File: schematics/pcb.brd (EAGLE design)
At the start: 69.8 x 100 mm, 39 parts, among them IC1 7805TV, IC2 4050D, IC3 LP298XS, Q1 16Mhz, Q2 16Mhz, X1 MICROSD

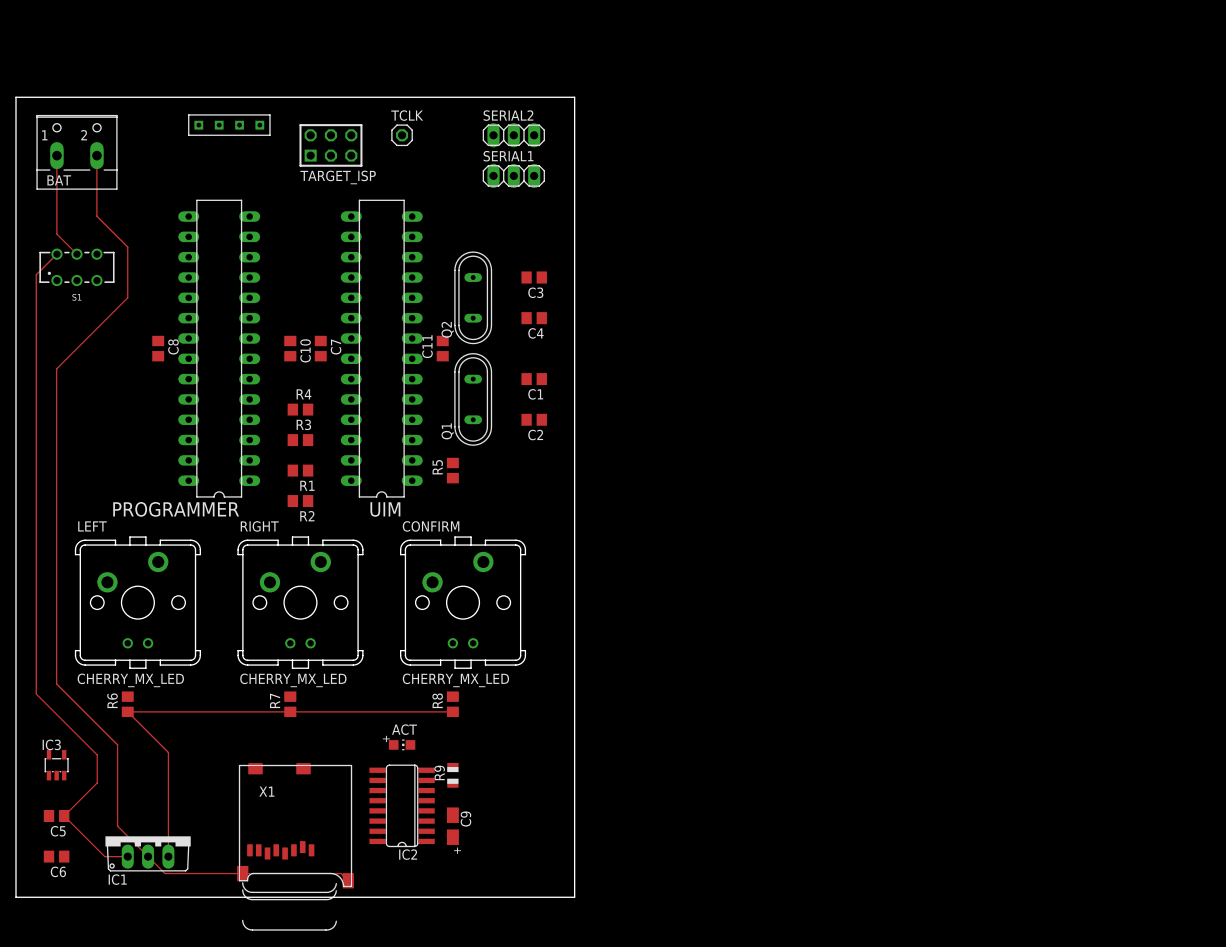
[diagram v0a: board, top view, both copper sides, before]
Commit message: Updated OLED module in part library; Scraped current PCB placements
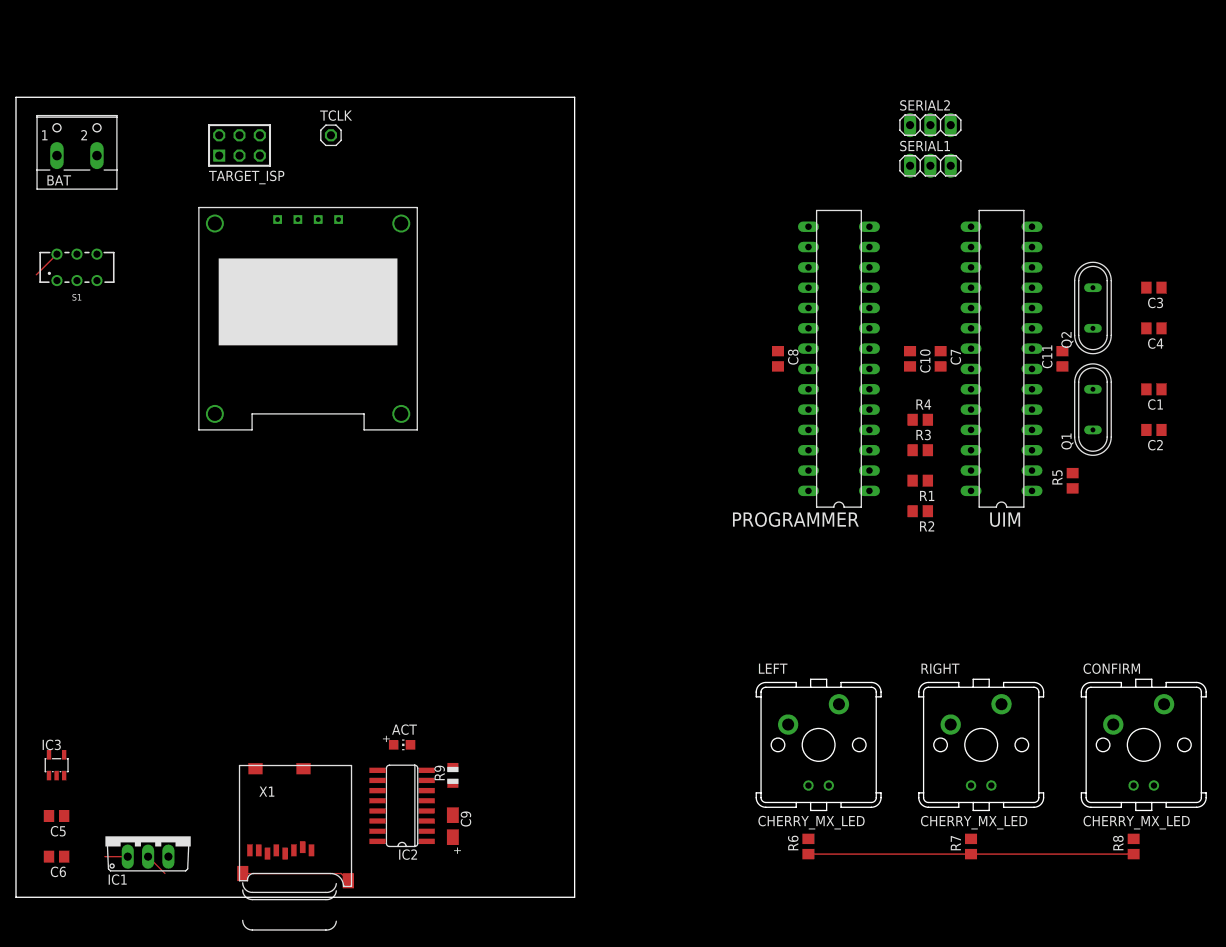
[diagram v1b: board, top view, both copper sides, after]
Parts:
- moved CONFIRM 86.9 mm to (141.0, 19.1)
- moved LEFT 86.9 mm to (100.3, 19.1)
- moved R6 86.9 mm to (99.1, 6.35)
- moved R7 86.9 mm to (119.4, 6.35)
- moved RIGHT 86.9 mm to (120.7, 19.1)
- moved R8 86.9 mm to (139.7, 6.35)
- moved C1 77.5 mm to (142.2, 63.5)
- moved C2 77.5 mm to (142.2, 58.4)
- moved C3 77.5 mm to (142.2, 76.2)
- moved C4 77.5 mm to (142.2, 71.1)
- moved R5 77.5 mm to (132.1, 52.1)
- moved C10 77.5 mm to (111.8, 67.3)
- moved C11 77.5 mm to (130.8, 67.3)
- moved C7 77.5 mm to (115.6, 67.3)
- moved C8 77.5 mm to (95.2, 67.3)
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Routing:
- net GND: track 123.9 -> 16.6 mm
- net PWRIN: track 86.2 -> 6.51 mm
- net +5V: track 60.8 -> 40.6 mm
- net N$17: track 13.4 -> 0.00 mm

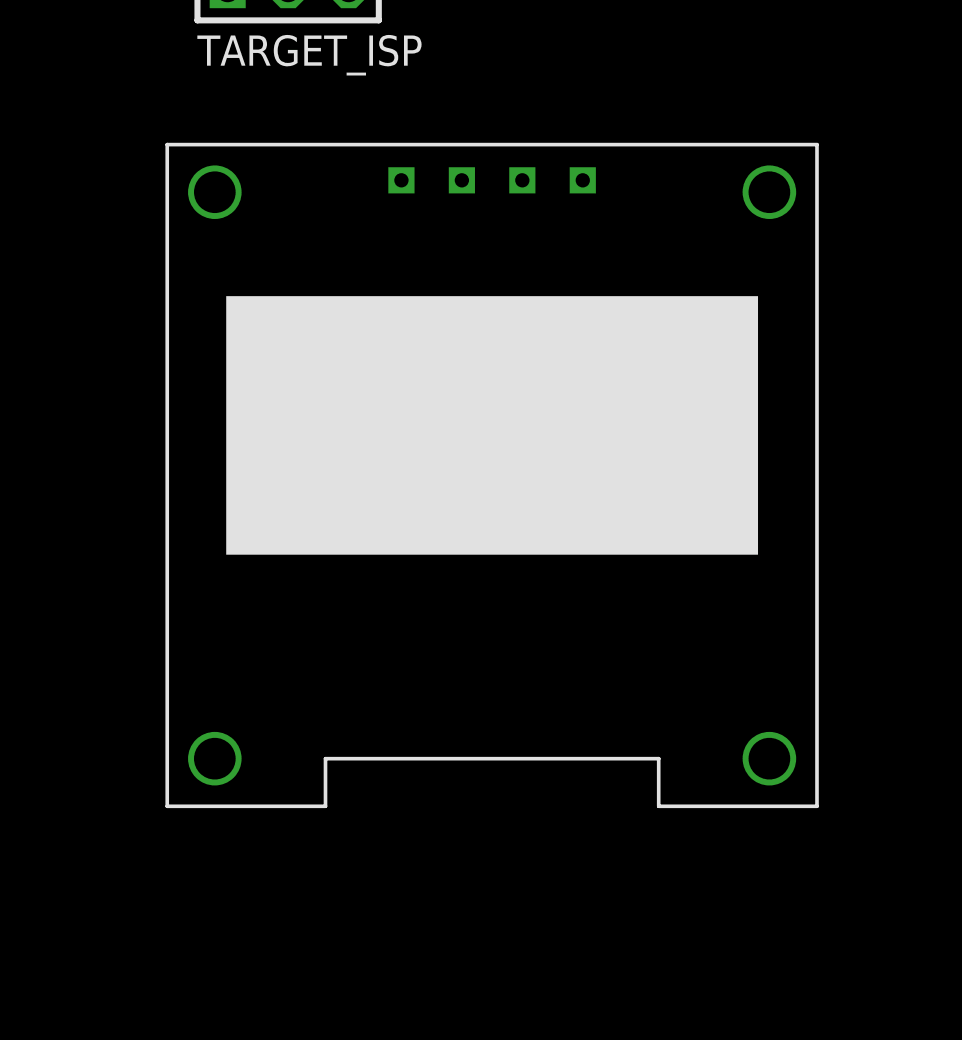
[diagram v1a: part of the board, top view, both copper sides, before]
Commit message: Further updates to OLED module
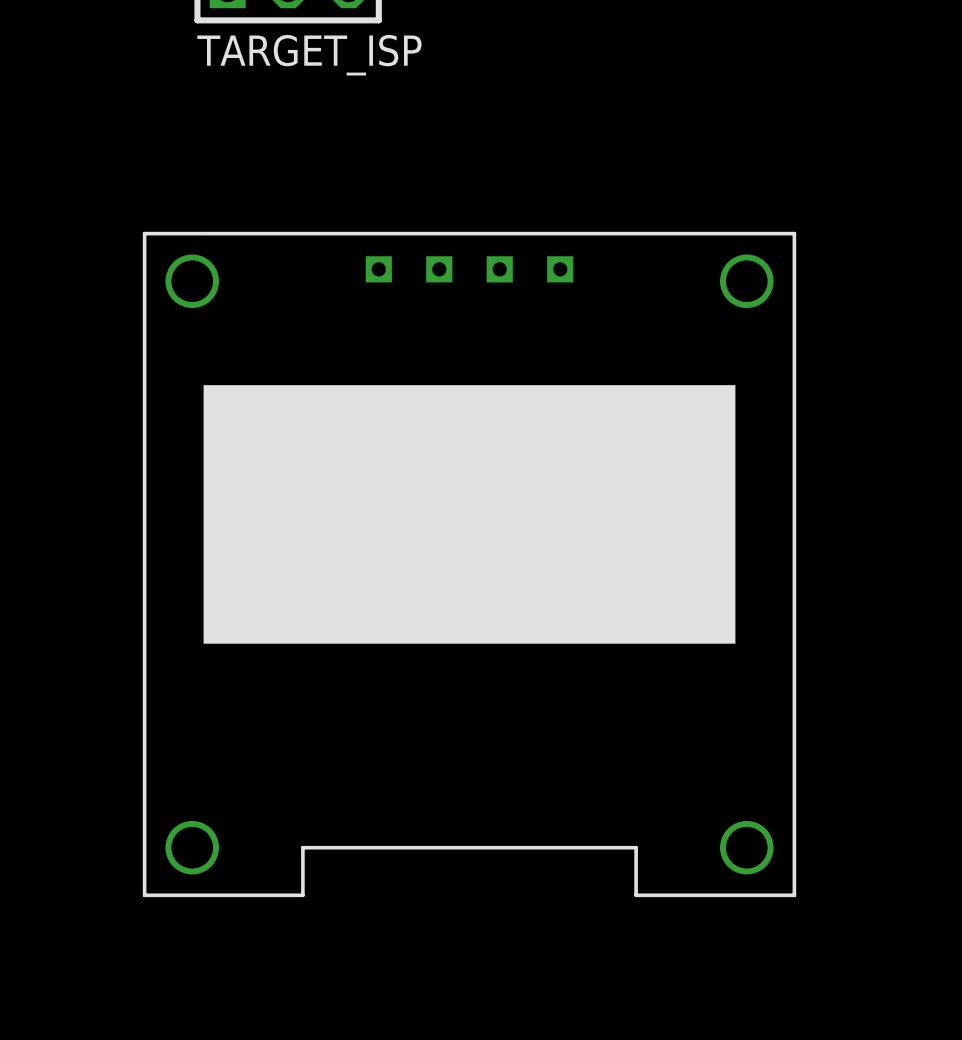
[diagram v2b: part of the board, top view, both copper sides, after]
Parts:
- moved U$1 16.3 mm to (35.6, 68.6)
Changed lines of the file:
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@@
 </autorouter>
 <elements>
-<element name="ACT" library="adafruit" package="CHIP-LED0805" value="RED" x="48.26" y="19.05" smashed="yes" rot="R270">
+<element name="ACT" library="adafruit" library_urn="urn:adsk.eagle:library:420" package="CHIP-LED0805" package3d_urn="urn:adsk.eagle:package:6240557/1" value="RED" x="48.26" y="19.05" smashed="yes" rot="R270">
 <attribute name="NAME" x="46.99" y="20.32" size="1.27" layer="25"/>
 <attribute name="VALUE" x="46.99" y="16.51" size="1.27" layer="27"/>
@@
 <attribute name="VALUE" x="92.71" y="68.58" size="1.27" layer="27" rot="R270"/>
 </element>
-<element name="C9" library="adafruit" package="A/3216-18R" value="10uF" x="54.61" y="8.89" smashed="yes" rot="R270">
+<element name="C9" library="adafruit" library_urn="urn:adsk.eagle:library:420" package="A/3216-18R" package3d_urn="urn:adsk.eagle:package:6240466/1" value="10uF" x="54.61" y="8.89" smashed="yes" rot="R270">
 <attribute name="NAME" x="55.61" y="10.84" size="1.27" layer="25" rot="R270"/>
 <attribute name="VALUE" x="52.285" y="10.84" size="1.27" layer="27" rot="R270"/>
@@
 <attribute name="VALUE" x="11.43" y="0" size="1.27" layer="27" ratio="10"/>
 </element>
-<element name="IC2" library="40xx" package="SO16" value="4050D" x="48.26" y="11.43" smashed="yes" rot="R90">
+<element name="IC2" library="40xx" library_urn="urn:adsk.eagle:library:80" package="SO16" package3d_urn="urn:adsk.eagle:package:821/2" value="4050D" x="48.26" y="11.43" smashed="yes" rot="R90">
 <attribute name="NAME" x="50.292" y="5.969" size="1.27" layer="25" ratio="10" rot="R180"/>
+<attribute name="POPULARITY" value="6" x="48.26" y="11.43" size="1.778" layer="27" rot="R90" display="off"/>
 <attribute name="VALUE" x="48.895" y="7.366" size="1.27" layer="27" ratio="10" rot="R90"/>
 </element>
-<element name="IC3" library="adafruit" package="SOT23-5L" value="LP298XS" x="5.08" y="16.51" smashed="yes">
+<element name="IC3" library="adafruit" library_urn="urn:adsk.eagle:library:420" package="SOT23-5L" package3d_urn="urn:adsk.eagle:package:6240724/1" value="LP298XS" x="5.08" y="16.51" smashed="yes">
 <attribute name="NAME" x="3.175" y="18.415" size="1.27" layer="25"/>
 <attribute name="VALUE" x="3.175" y="13.081" size="1.27" layer="27"/>
@@
 <attribute name="VALUE" x="142.24" y="5.715" size="1.27" layer="27" rot="R90"/>
 </element>
-<element name="R9" library="adafruit" package="R0805" value="1K" x="54.61" y="15.24" smashed="yes" rot="R90">
+<element name="R9" library="adafruit" library_urn="urn:adsk.eagle:library:420" package="R0805" package3d_urn="urn:adsk.eagle:package:6240566/1" value="1K" x="54.61" y="15.24" smashed="yes" rot="R90">
 <attribute name="NAME" x="53.594" y="14.478" size="1.27" layer="25" rot="R90"/>
 <attribute name="VALUE" x="56.896" y="14.478" size="1.27" layer="27" rot="R90"/>
@@
 <attribute name="VALUE" x="38.1" y="92.075" size="1.27" layer="27"/>
 </element>
-<element name="U$1" library="Parts" package="128X64-I2C-OLED" value="128X64-I2C-OLED" x="22.86" y="58.42" smashed="yes"/>
+<element name="U$1" library="Parts" package="128X64-I2C-OLED" value="128X64-I2C-OLED" x="35.56" y="68.58" smashed="yes"/>
 <element name="UIM" library="atmega8" package="DIL28-3" value="ATMEGA48/88/168-PU" x="123.19" y="67.31" smashed="yes" rot="R90">
 <attribute name="NAME" x="125.73" y="48.1076" size="1.778" layer="25" ratio="10" rot="R180"/>
 <attribute name="VALUE" x="123.825" y="51.435" size="1.778" layer="27" ratio="10" rot="R90"/>
 </element>
-<element name="X1" library="adafruit" package="MICROSD" value="MICROSD" x="27.94" y="16.51" smashed="yes">
+<element name="X1" library="adafruit" library_urn="urn:adsk.eagle:library:420" package="MICROSD" package3d_urn="urn:adsk.eagle:package:6240723/1" value="MICROSD" x="27.94" y="16.51" smashed="yes">
 <attribute name="NAME" x="30.37" y="12.57" size="1.27" layer="25"/>
 </element>
@@
 <wire x1="4.13" y1="10.16" x2="4.13" y2="5.08" width="0" layer="19" extent="1-1"/>
 <wire x1="5.08" y1="15.21" x2="4.13" y2="10.16" width="0" layer="19" extent="1-1"/>
-<wire x1="30.48" y1="95.25" x2="95.25" y2="66.36" width="0" layer="19" extent="1-1"/>
-<wire x1="32.7" y1="84.72" x2="30.48" y2="95.25" width="0" layer="19" extent="1-1"/>
-<wire x1="10.12" y1="92.71" x2="32.7" y2="84.72" width="0" layer="19" extent="1-1"/>
+<wire x1="31.75" y1="80.98" x2="5.08" y2="15.21" width="0" layer="19" extent="1-1"/>
+<wire x1="10.12" y1="92.71" x2="31.75" y2="80.98" width="0" layer="19" extent="1-1"/>
+<wire x1="30.48" y1="95.25" x2="10.12" y2="92.71" width="0" layer="19" extent="1-1"/>
 </signal>
 <signal name="+5V">
@@
 <wire x1="132.08" y1="53.02" x2="130.81" y2="66.36" width="0" layer="19" extent="1-1"/>
 <wire x1="139.7" y1="5.4" x2="132.08" y2="53.02" width="0" layer="19" extent="1-1"/>
-<wire x1="35.24" y1="84.72" x2="99.06" y2="71.12" width="0" layer="19" extent="1-1"/>
-<wire x1="25.4" y1="95.25" x2="35.24" y2="84.72" width="0" layer="19" extent="1-1"/>
-<wire x1="6.03" y1="15.21" x2="35.24" y2="84.72" width="0" layer="19" extent="1-1"/>
+<wire x1="34.29" y1="80.98" x2="99.06" y2="71.12" width="0" layer="19" extent="1-1"/>
+<wire x1="25.4" y1="95.25" x2="34.29" y2="80.98" width="0" layer="19" extent="1-1"/>
+<wire x1="6.03" y1="15.21" x2="34.29" y2="80.98" width="0" layer="19" extent="1-1"/>
 <wire x1="4.13" y1="15.21" x2="6.03" y2="15.21" width="0" layer="19" extent="1-1"/>
 <wire x1="6.03" y1="5.08" x2="6.03" y2="15.21" width="0" layer="19" extent="1-1"/>
@@
 <contactref element="R2" pad="1"/>
 <contactref element="U$1" pad="SCL"/>
-<wire x1="119.38" y1="50.8" x2="37.78" y2="84.72" width="0" layer="19" extent="1-1"/>
 <wire x1="113.98" y1="48.26" x2="119.38" y2="50.8" width="0" layer="19" extent="1-1"/>
 <wire x1="99.06" y1="50.8" x2="113.98" y2="48.26" width="0" layer="19" extent="1-1"/>
+<wire x1="36.83" y1="80.98" x2="99.06" y2="50.8" width="0" layer="19" extent="1-1"/>
 </signal>
 <signal name="N$2">
@@
 <contactref element="R1" pad="1"/>
 <contactref element="U$1" pad="SDA"/>
-<wire x1="119.38" y1="53.34" x2="40.32" y2="84.72" width="0" layer="19" extent="1-1"/>
 <wire x1="113.98" y1="52.07" x2="119.38" y2="53.34" width="0" layer="19" extent="1-1"/>
 <wire x1="99.06" y1="53.34" x2="113.98" y2="52.07" width="0" layer="19" extent="1-1"/>
+<wire x1="39.37" y1="80.98" x2="99.06" y2="53.34" width="0" layer="19" extent="1-1"/>
 </signal>
 <signal name="N$3">
@@
 <contactref element="R5" pad="1"/>
 <contactref element="SERIAL1" pad="1"/>
-<wire x1="132.08" y1="51.12" x2="111.76" y2="91.44" width="0" layer="19" extent="1-1"/>
-<wire x1="127" y1="50.8" x2="132.08" y2="51.12" width="0" layer="19" extent="1-1"/>
+<wire x1="127" y1="50.8" x2="111.76" y2="91.44" width="0" layer="19" extent="1-1"/>
+<wire x1="132.08" y1="51.12" x2="127" y2="50.8" width="0" layer="19" extent="1-1"/>
 </signal>
 <signal name="N$7">
@@
 <contactref element="PROGRAMMER" pad="11"/>
 <contactref element="TARGET_ISP" pad="4"/>
-<wire x1="106.68" y1="76.2" x2="27.94" y2="95.25" width="0" layer="19" extent="1-1"/>
+<wire x1="27.94" y1="95.25" x2="106.68" y2="76.2" width="0" layer="19" extent="1-1"/>
 </signal>
 <signal name="N$12">
 <contactref element="PROGRAMMER" pad="12"/>
 <contactref element="TARGET_ISP" pad="1"/>
-<wire x1="106.68" y1="78.74" x2="25.4" y2="92.71" width="0" layer="19" extent="1-1"/>
+<wire x1="25.4" y1="92.71" x2="106.68" y2="78.74" width="0" layer="19" extent="1-1"/>
 </signal>
 <signal name="N$13">
 <contactref element="PROGRAMMER" pad="13"/>
 <contactref element="TARGET_ISP" pad="3"/>
-<wire x1="106.68" y1="81.28" x2="27.94" y2="92.71" width="0" layer="19" extent="1-1"/>
+<wire x1="27.94" y1="92.71" x2="106.68" y2="81.28" width="0" layer="19" extent="1-1"/>
 </signal>
 <signal name="N$14">
 <contactref element="TARGET_ISP" pad="5"/>
 <contactref element="PROGRAMMER" pad="6"/>
-<wire x1="106.68" y1="63.5" x2="30.48" y2="92.71" width="0" layer="19" extent="1-1"/>
+<wire x1="30.48" y1="92.71" x2="106.68" y2="63.5" width="0" layer="19" extent="1-1"/>
 </signal>
 <signal name="N$9">
@@
 <contactref element="PROGRAMMER" pad="16"/>
 <contactref element="TCLK" pad="1"/>
-<wire x1="99.06" y1="81.28" x2="39.37" y2="95.25" width="0" layer="19" extent="1-1"/>
+<wire x1="39.37" y1="95.25" x2="99.06" y2="81.28" width="0" layer="19" extent="1-1"/>
 </signal>
 <signal name="N$29">
